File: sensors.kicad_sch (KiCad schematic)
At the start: 2 parts, among them U4 BMP390, U5 ICM-42670-P

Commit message: Power circuitry
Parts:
- U4: footprint 10LGA_2X2X0p75_BOS -> BMP390:10LGA_2X2X0p75_BOS
- U5: footprint LGA14_2.5X3X0.76_IVS -> ICM-42670-P:LGA14_2.5X3X0.76_IVS
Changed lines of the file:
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@@
 			)
 		)
-		(property "Footprint" "10LGA_2X2X0p75_BOS"
+		(property "Footprint" "BMP390:10LGA_2X2X0p75_BOS"
 			(at 104.14 77.47 0)
 			(effects
@@
 			)
 		)
-		(property "Footprint" "LGA14_2.5X3X0.76_IVS"
+		(property "Footprint" "ICM-42670-P:LGA14_2.5X3X0.76_IVS"
 			(at 102.87 100.076 0)
 			(effects

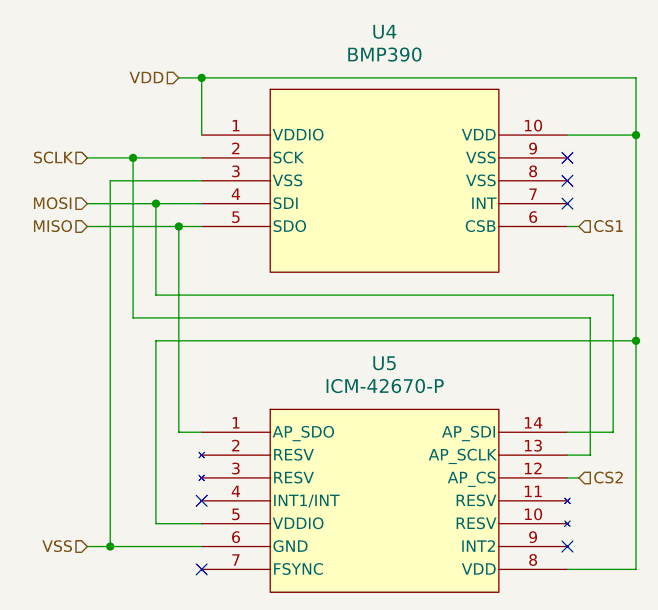
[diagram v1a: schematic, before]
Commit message: Update references and switch to higher power MOSFETS
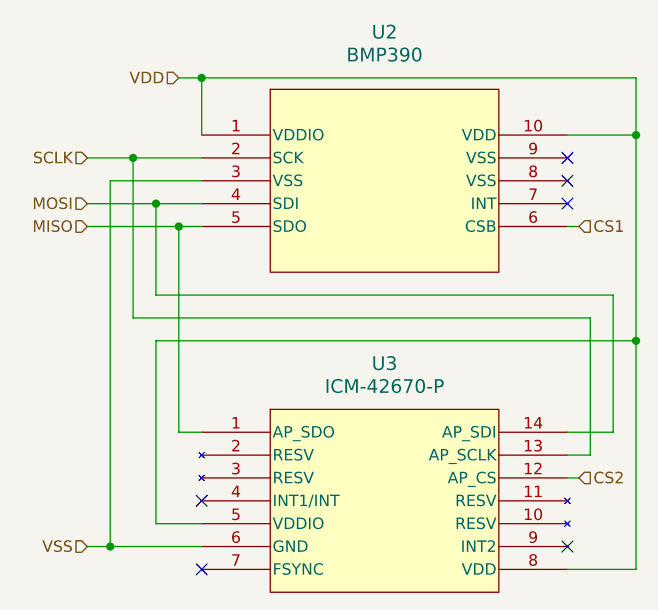
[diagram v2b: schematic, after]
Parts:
- renumbered U4 to U2, U5 to U3
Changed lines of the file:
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@@
 		(on_board yes)
 		(dnp no)
-		(property "Reference" "U4"
+		(property "Reference" "U2"
 			(at 124.46 66.04 0)
 			(effects
@@
 			(project "rocket"
 				(path "/d94d1fd0-ec09-478b-a1a4-3306111fc872/157fcf70-07f6-4699-a0dc-76a38178ab0a"
-					(reference "U4")
+					(reference "U2")
 					(unit 1)
 				)
@@
 		(dnp no)
 		(fields_autoplaced yes)
-		(property "Reference" "U5"
+		(property "Reference" "U3"
 			(at 124.46 102.87 0)
 			(effects
@@
 			(project "rocket"
 				(path "/d94d1fd0-ec09-478b-a1a4-3306111fc872/157fcf70-07f6-4699-a0dc-76a38178ab0a"
-					(reference "U5")
+					(reference "U3")
 					(unit 1)
 				)
